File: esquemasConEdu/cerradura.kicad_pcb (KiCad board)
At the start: 2 copper layers, 87.7 x 141.8 mm, 16 parts, among them T1 BC547

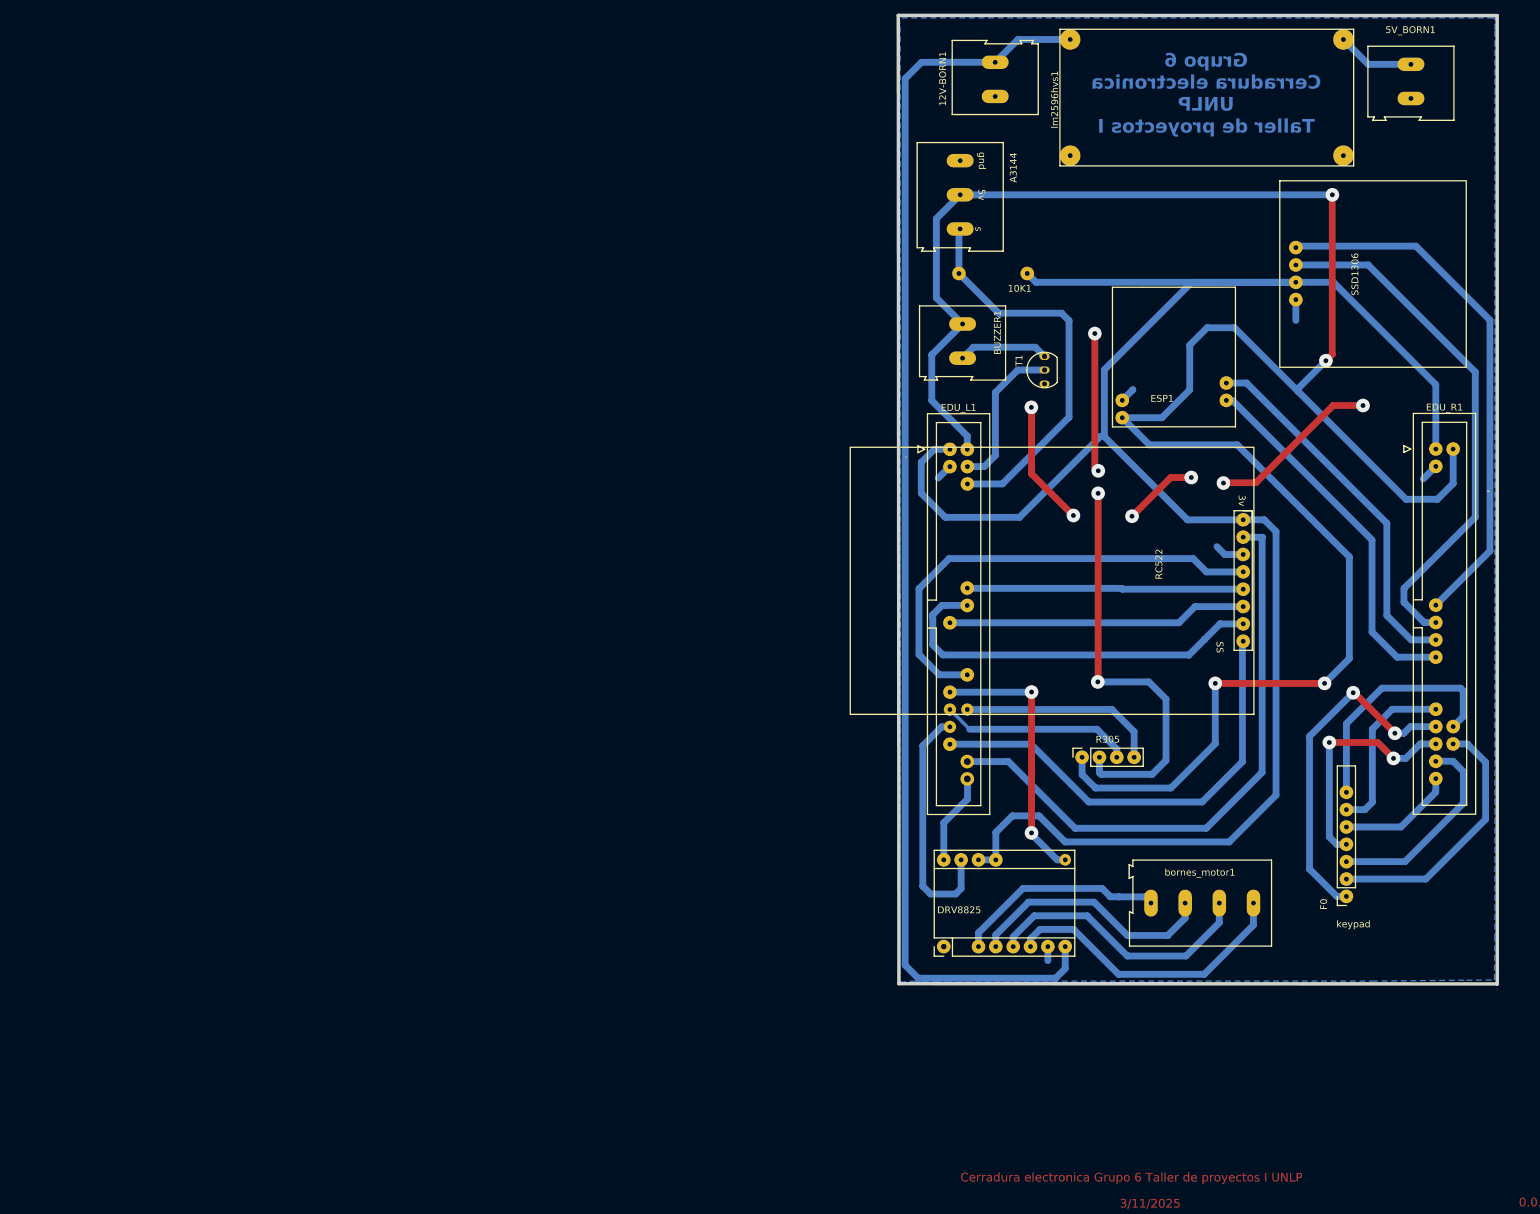
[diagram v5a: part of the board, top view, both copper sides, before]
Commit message: se agrega modulo de deteccion de presencia y resistencia en base de T1
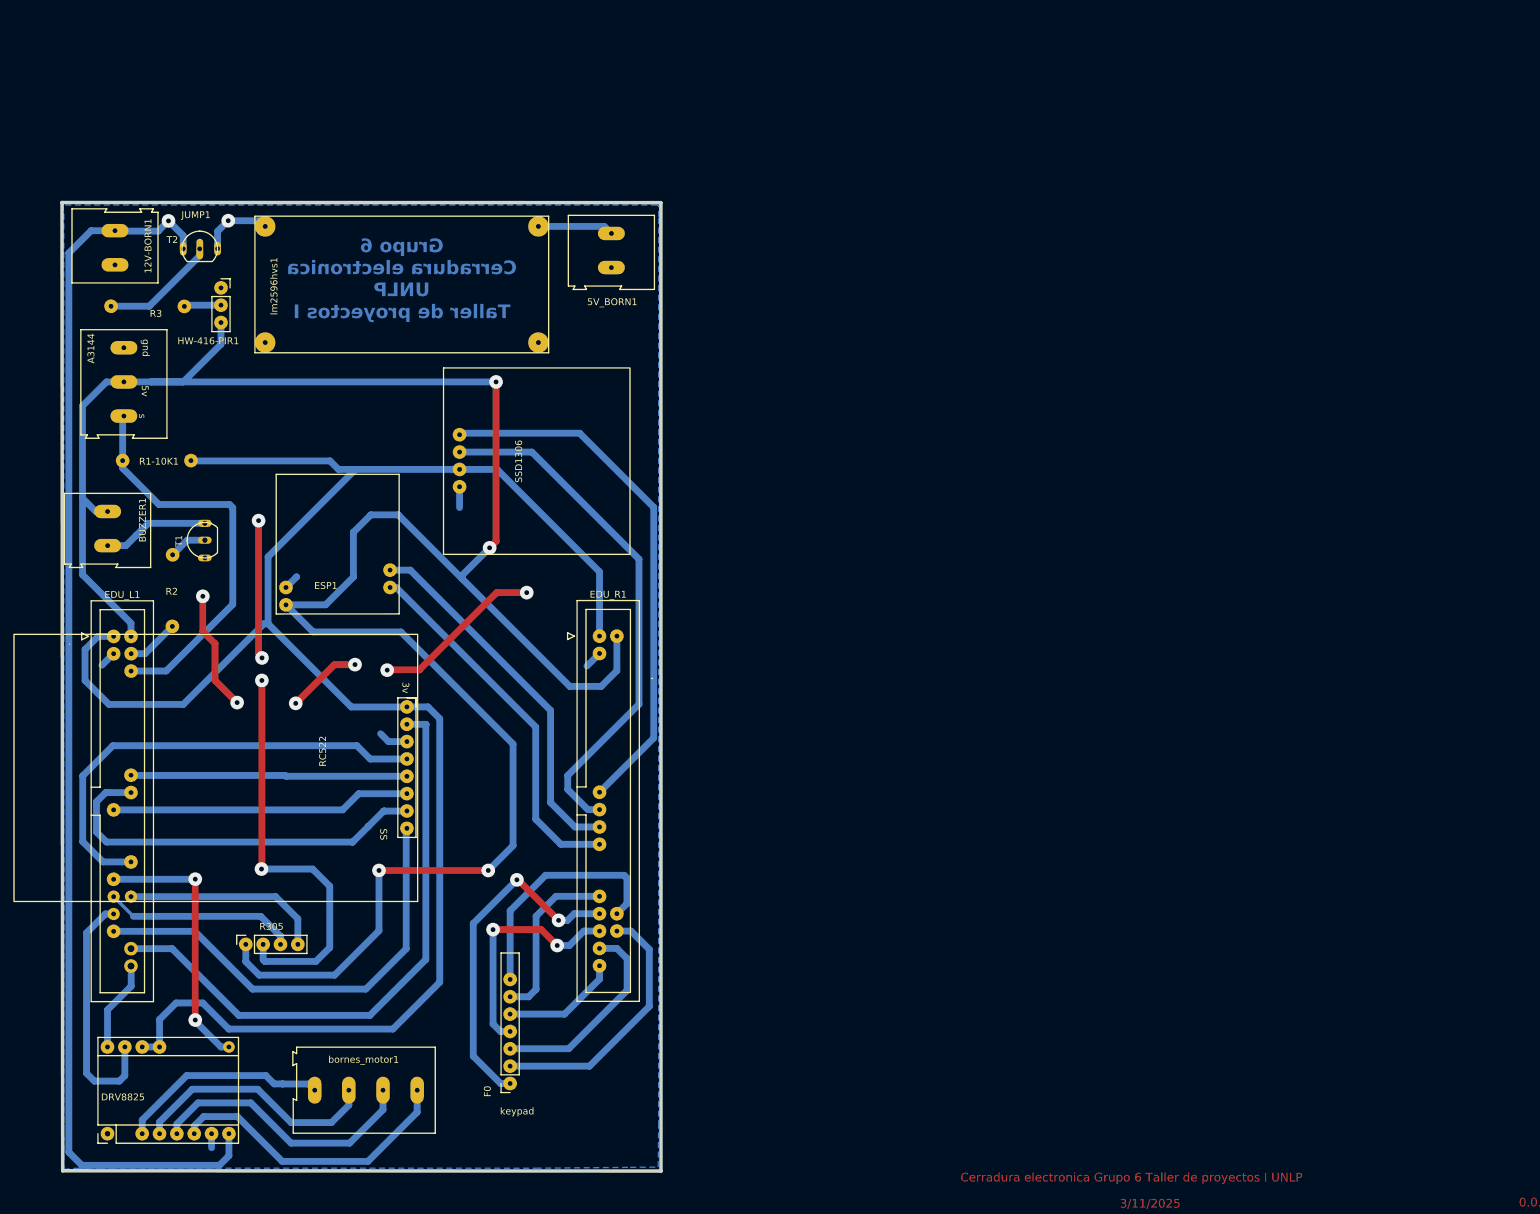
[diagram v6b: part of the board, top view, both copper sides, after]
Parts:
- added HW-416-PIR1: HW-416-PIR, Connector_PinSocket_2.54mm:PinSocket_1x03_P2.54mm_Vertical, F.Cu at (82.2, 59.1)
- added R2: R2, Connector_PinHeader_1.00mm:PinHeader_1x02_P1.00mm_Vertical, F.Cu at (75.0, 103.6)
- added R3: R3, Connector_PinHeader_1.00mm:PinHeader_1x02_P1.00mm_Vertical, F.Cu at (71.5, 61.8)
- added T2: BC547, Package_TO_SOT_THT:TO-92_Inline, F.Cu at (77.8, 53.4)
- R1-10K1: renamed from 10K1; value 10K -> R1 (10k)
- moved 12V-BORN1 131.2 mm to (66.7, 55.8)
- moved BUZZER1 128.1 mm to (65.6, 91.9)
- moved RC522 125.5 mm to (109.5, 138.3)
- moved num_keypad1 125.5 mm to (124.5, 175.6)
- moved A3144 125.5 mm to (68.0, 67.9)
- moved DRV8825 125.5 mm to (65.6, 183.0)
- moved EDU_L1 125.5 mm to (66.5, 110.2)
- moved EDU_R1 125.5 mm to (137.6, 110.1)
- moved ESP1 125.5 mm to (104.4, 105.5)
- moved R305 125.5 mm to (85.8, 155.2)
- moved SSD1306 125.5 mm to (117.1, 80.6)
- moved bornes_motor1 125.5 mm to (110.9, 176.6)
- moved R1-10K1 125.5 mm to (76.8, 84.4)
- moved T1 125.4 mm to (79.8, 97.3)
- moved lm2596hvs1 121.0 mm to (108.7, 57.6)
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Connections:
- T1 pad 2: /buzzer_sgn -> Net-(T1-B)
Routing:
- net +5V: track 315.9 -> 336.0 mm
- net Net-(T2-B): track 0.00 -> 17.1 mm
- net /buzzer_sgn: track 22.6 -> 7.69 mm
- net +3.3V: track 284.7 -> 270.5 mm
- net +12V: track 184.4 -> 191.8 mm, vias 0 -> 2
- net Net-(T1-B): track 0.00 -> 5.61 mm
- net /hw-416-sgn: track 0.00 -> 5.43 mm
- net Net-(BUZZER1-Pin_2): track 13.2 -> 15.6 mm
- net GND: track 152.1 -> 151.4 mm
- net /door_sensor: track 58.9 -> 59.6 mm
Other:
- board text added: "JUMP1"

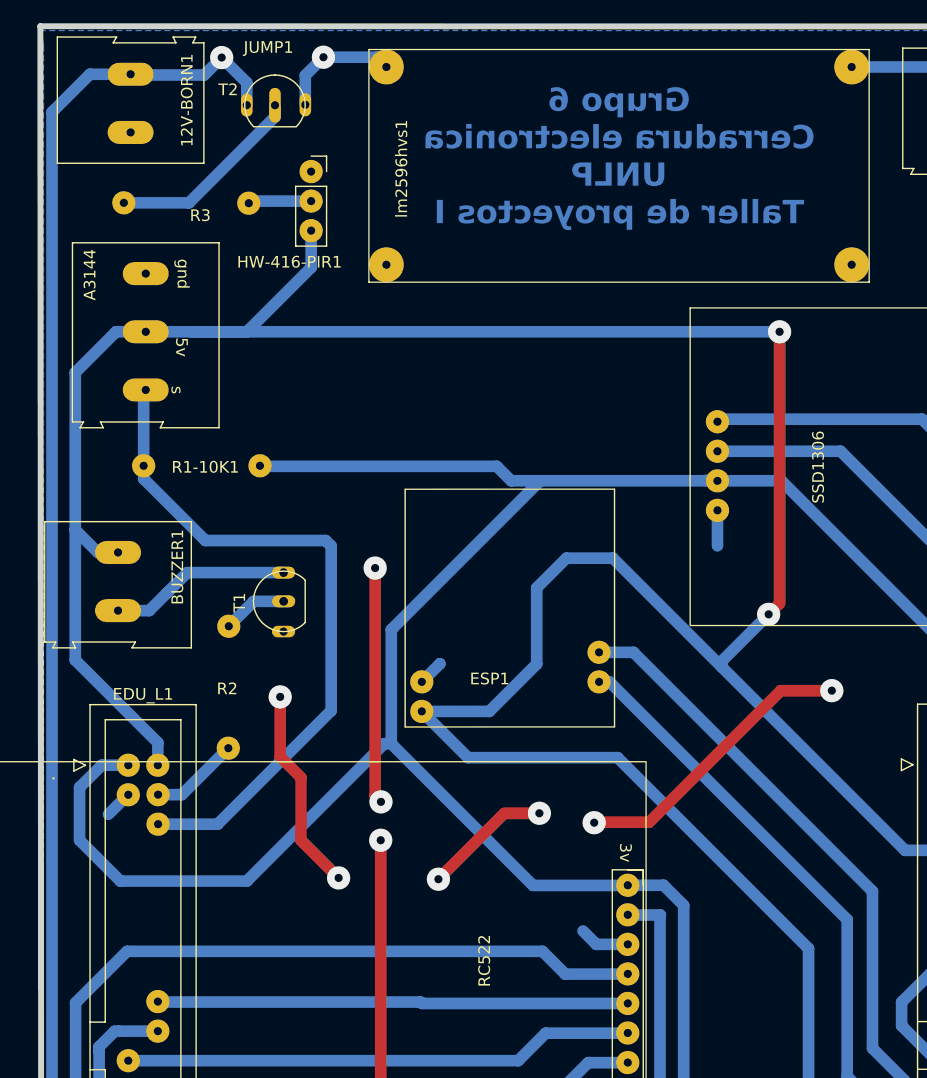
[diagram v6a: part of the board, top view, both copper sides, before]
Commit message: sensor de presencia con gpio
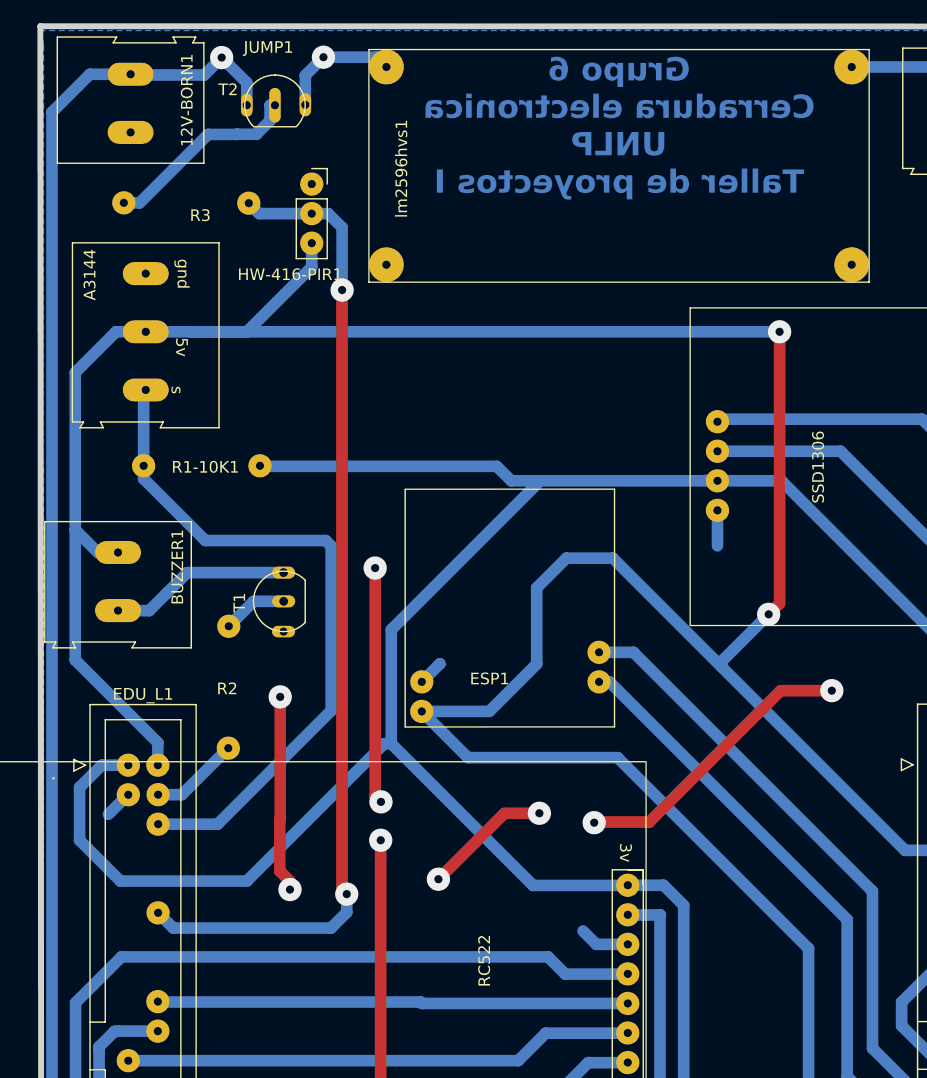
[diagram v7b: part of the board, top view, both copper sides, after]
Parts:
- moved HW-416-PIR1 1.08 mm to (82.2, 60.2)
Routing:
- net /hw-416-sgn: track 5.43 -> 85.2 mm, vias 0 -> 2
- net +5V: track 336.0 -> 334.9 mm
- net GND: track 151.4 -> 150.6 mm
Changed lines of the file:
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@@
 	(footprint "Connector_PinSocket_2.54mm:PinSocket_1x03_P2.54mm_Vertical"
 		(layer "F.Cu")
-		(at 82.1875 59.115)
+		(at 82.24 60.19)
 		(descr "Through hole straight socket strip, 1x03, 2.54mm pitch, single row (from Kicad 4.0.7), script generated")
 		(tags "Through hole socket strip THT 1x03 2.54mm single row")
@@
 			(pintype "passive")
 		)
+		(pad "12" thru_hole circle
+			(at 2.56 12.69)
+			(size 2 2)
+			(drill 0.7)
+			(layers "*.Cu" "B.Mask")
+			(remove_unused_layers no)
+			(net 36 "/hw-416-sgn")
+			(pinfunction "Pin_12")
+			(pintype "passive")
+		)
 		(pad "18" thru_hole circle
 			(at 2.54 20.32)
@@
 	)
 	(gr_text "Grupo 6 \nCerradura electronica\nUNLP \nTaller de proyectos I"
-		(at 108.6575 63.795 0)
+		(at 108.66 61.18 0)
 		(layer "B.Cu")
 		(effects
@@
 	)
 	(segment
+		(start 82.24 67.3125)
+		(end 76.6625 72.89)
+		(width 1)
+		(layer "B.Cu")
+		(net 4)
+	)
+	(segment
 		(start 101.58 94.9)
 		(end 104.13 92.35)
@@
 	)
 	(segment
+		(start 76.6625 72.89)
+		(end 71.9575 72.89)
+		(width 1)
+		(layer "B.Cu")
+		(net 4)
+	)
+	(segment
 		(start 121.52 97.18)
 		(end 117.495 101.205)
@@
 	)
 	(segment
+		(start 82.24 65.27)
+		(end 82.24 67.3125)
+		(width 1)
+		(layer "B.Cu")
+		(net 4)
+	)
+	(segment
 		(start 117.495 101.205)
 		(end 117.495 101.715)
@@
 	)
 	(segment
-		(start 82.1875 67.365)
-		(end 76.6625 72.89)
-		(width 1)
-		(layer "B.Cu")
-		(net 4)
-	)
-	(segment
 		(start 122.46 72.89)
 		(end 71.9575 72.89)
@@
 	)
 	(segment
-		(start 82.1875 64.195)
-		(end 82.1875 67.365)
-		(width 1)
-		(layer "B.Cu")
-		(net 4)
-	)
-	(segment
 		(start 63.857 91.86)
 		(end 61.912 89.915)
@@
 	)
 	(segment
-		(start 76.6625 72.89)
-		(end 71.9575 72.89)
-		(width 1)
-		(layer "B.Cu")
-		(net 4)
-	)
-	(segment
 		(start 108.13 92.35)
 		(end 117.495 101.715)
@@
 	)
 	(segment
-		(start 84.55 119.84)
-		(end 81.3175 116.6075)
+		(start 101.81 114.28)
+		(end 101.8 114.29)
+		(width 1)
+		(layer "F.Cu")
+		(net 5)
+	)
+	(segment
+		(start 80.37 120.84)
+		(end 80.37 120.13)
 		(width 1)
 		(layer "F.Cu")
@@
 	)
 	(segment
-		(start 101.81 114.28)
-		(end 101.8 114.29)
+		(start 80.37 120.13)
+		(end 79.5 119.26)
 		(width 1)
 		(layer "F.Cu")
@@
 	)
 	(segment
-		(start 81.3175 111.215)
-		(end 79.5275 109.425)
+		(start 79.5275 114.8175)
+		(end 79.5275 104.275)
 		(width 1)
 		(layer "F.Cu")
@@
 	)
 	(segment
-		(start 106.52 115.09)
-		(end 106.57 115.04)
+		(start 79.5 114.845)
+		(end 79.5275 114.8175)
 		(width 1)
 		(layer "F.Cu")
@@
 	)
 	(segment
-		(start 79.5275 109.425)
-		(end 79.5275 104.275)
+		(start 79.5 119.26)
+		(end 79.5 114.845)
+		(width 1)
+		(layer "F.Cu")
+		(net 5)
+	)
+	(segment
+		(start 106.52 115.09)
+		(end 106.57 115.04)
 		(width 1)
 		(layer "F.Cu")
@@
 	)
 	(segment
-		(start 81.3175 116.6075)
-		(end 81.3175 111.215)
-		(width 1)
-		(layer "F.Cu")
-		(net 5)
-	)
-	(segment
 		(start 106.57 115.04)
 		(end 111.26 115.04)
@@
 	)
 	(segment
-		(start 84.5 119.84)
-		(end 84.55 119.84)
-		(width 1)
-		(layer "F.Cu")
-		(net 5)
-	)
-	(segment
 		(start 111.26 115.04)
 		(end 122.56 103.74)
@@
 	)
 	(via
-		(at 84.55 119.84)
+		(at 80.37 120.84)
 		(size 2)
 		(drill 0.7)
@@
 	)
 	(segment
-		(start 69.01 143.17)
-		(end 64.91 143.17)
+		(start 102.56 126.63)
+		(end 104.035 128.105)
 		(width 1)
 		(layer "B.Cu")
@@
 	)
 	(segment
-		(start 61.94 130.57)
-		(end 66.36 126.15)
+		(start 65.88 126.63)
+		(end 102.56 126.63)
 		(width 1)
 		(layer "B.Cu")
@@
 	)
 	(segment
-		(start 104.035 128.105)
-		(end 109.3 128.105)
+		(start 61.94 130.57)
+		(end 65.88 126.63)
 		(width 1)
 		(layer "B.Cu")
@@
 	)
 	(segment
-		(start 64.91 143.17)
-		(end 61.94 140.2)
+		(start 61.94 140.2)
+		(end 61.94 130.57)
 		(width 1)
 		(layer "B.Cu")
@@
 	)
 	(segment
-		(start 66.36 126.15)
-		(end 102.08 126.15)
+		(start 104.035 128.105)
+		(end 109.3 128.105)
 		(width 1)
 		(layer "B.Cu")
@@
 	)
 	(segment
-		(start 102.08 126.15)
-		(end 104.035 128.105)
+		(start 64.91 143.17)
+		(end 61.94 140.2)
 		(width 1)
 		(layer "B.Cu")
@@
 	)
 	(segment
-		(start 61.94 140.2)
-		(end 61.94 130.57)
+		(start 69.01 143.17)
+		(end 64.91 143.17)
 		(width 1)
 		(layer "B.Cu")
@@
 	)
 	(segment
-		(start 77.0075 61.655)
-		(end 82.1875 61.655)
+		(start 84.85 120.83)
+		(end 84.85 69.3)
+		(width 1)
+		(layer "F.Cu")
+		(net 36)
+	)
+	(segment
+		(start 85.25 121.23)
+		(end 84.85 120.83)
+		(width 1)
+		(layer "F.Cu")
+		(net 36)
+	)
+	(via
+		(at 85.25 121.23)
+		(size 2)
+		(drill 0.7)
+		(layers "F.Cu" "B.Cu")
+		(free yes)
+		(net 36)
+	)
+	(via
+		(at 84.85 69.3)
+		(size 2)
+		(drill 0.7)
+		(layers "F.Cu" "B.Cu")
+		(free yes)
+		(net 36)
+	)
+	(segment
+		(start 85.25 121.23)
+		(end 85.25 122.8)
+		(width 1)
+		(layer "B.Cu")
+		(net 36)
+	)
+	(segment
+		(start 84.85 63.925787)
+		(end 84.85 69.3)
+		(width 1)
+		(layer "B.Cu")
+		(net 36)
+	)
+	(segment
+		(start 77.7225 62.73)
+		(end 82.24 62.73)
+		(width 1)
+		(layer "B.Cu")
+		(net 36)
+	)
+	(segment
+		(start 83.901 124.149)
+		(end 70.339 124.149)
+		(width 1)
+		(layer "B.Cu")
+		(net 36)
+	)
+	(segment
+		(start 83.654213 62.73)
+		(end 84.85 63.925787)
 		(width 1)
 		(layer "B.Cu")
@@
 	(segment
 		(start 76.8275 61.835)
-		(end 77.0075 61.655)
+		(end 77.7225 62.73)
+		(width 1)
+		(layer "B.Cu")
+		(net 36)
+	)
+	(segment
+		(start 70.339 124.149)
+		(end 69.03 122.84)
+		(width 1)
+		(layer "B.Cu")
+		(net 36)
+	)
+	(segment
+		(start 82.24 62.73)
+		(end 83.654213 62.73)
+		(width 1)
+		(layer "B.Cu")
+		(net 36)
+	)
+	(segment
+		(start 85.25 122.8)
+		(end 83.901 124.149)
 		(width 1)
 		(layer "B.Cu")
@@
 	)
 	(segment
+		(start 73.33 55.92)
+		(end 67.445 61.805)
+		(width 1)
+		(layer "B.Cu")
+		(net 37)
+	)
+	(segment
+		(start 67.445 61.805)
+		(end 66.0875 61.805)
+		(width 1)
+		(layer "B.Cu")
+		(net 37)
+	)
+	(segment
+		(start 78.6585 53.415)
+		(end 78.6585 54.733841)
+		(width 1)
+		(layer "B.Cu")
+		(net 37)
+	)
+	(segment
+		(start 75.814659 55.92)
+		(end 73.33 55.92)
+		(width 1)
+		(layer "B.Cu")
+		(net 37)
+	)
+	(segment
 		(start 79.0775 53.415)
-		(end 79.0775 54.415)
+		(end 78.6585 53.415)
 		(width 1)
 		(layer "B.Cu")
@@
 	)
 	(segment
-		(start 79.0775 54.415)
-		(end 71.6875 61.805)
+		(start 78.6585 54.733841)
+		(end 77.486341 55.906)
 		(width 1)
 		(layer "B.Cu")
@@
 	)
 	(segment
-		(start 71.6875 61.805)
-		(end 66.0875 61.805)
+		(start 77.486341 55.906)
+		(end 75.828659 55.906)
+		(width 1)
+		(layer "B.Cu")
+		(net 37)
+	)
+	(segment
+		(start 75.828659 55.906)
+		(end 75.814659 55.92)
 		(width 1)
 		(layer "B.Cu")
